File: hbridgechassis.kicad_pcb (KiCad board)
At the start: 2 copper layers, 100 x 100 mm, 8 parts, among them J1 Conn_01x02_Female, J2 Conn_01x02_Female, J3 Conn_01x02_Female, J4 Conn_01x07_Female, J5 Conn_01x02_Female, J6 Conn_01x02_Female, U1 L293DD

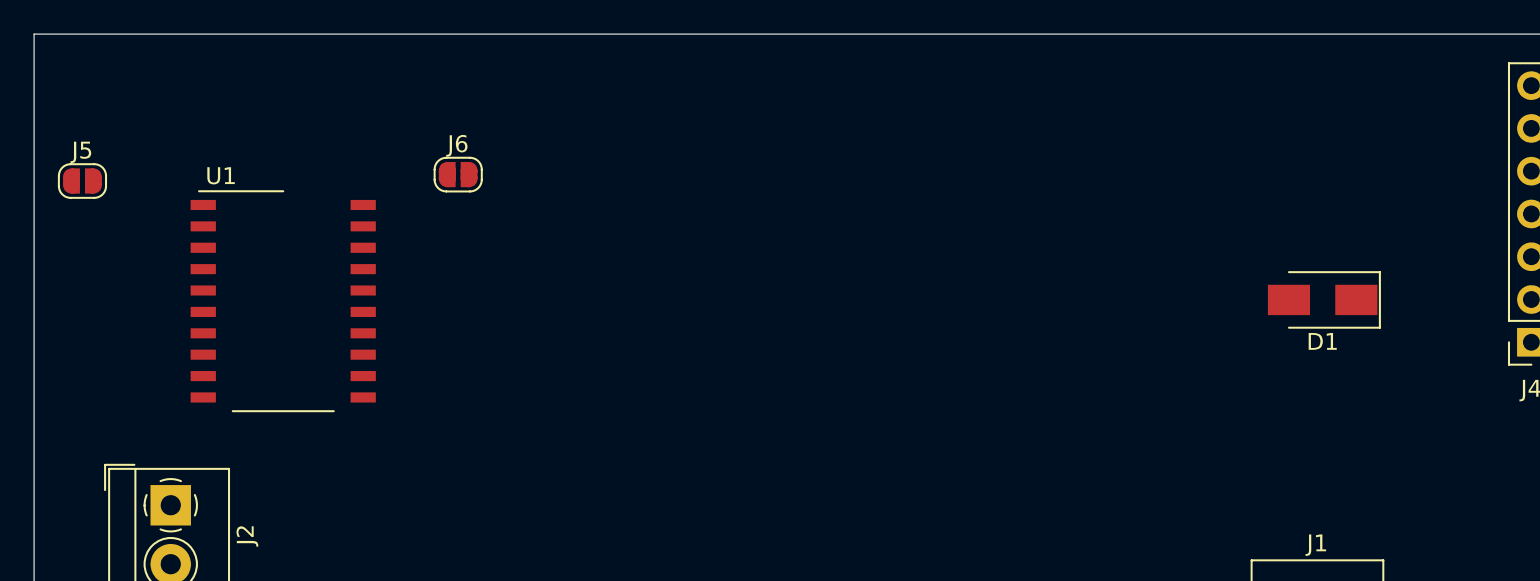
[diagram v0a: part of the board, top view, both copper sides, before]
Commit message: agregado regulador 78l05 y condensadores
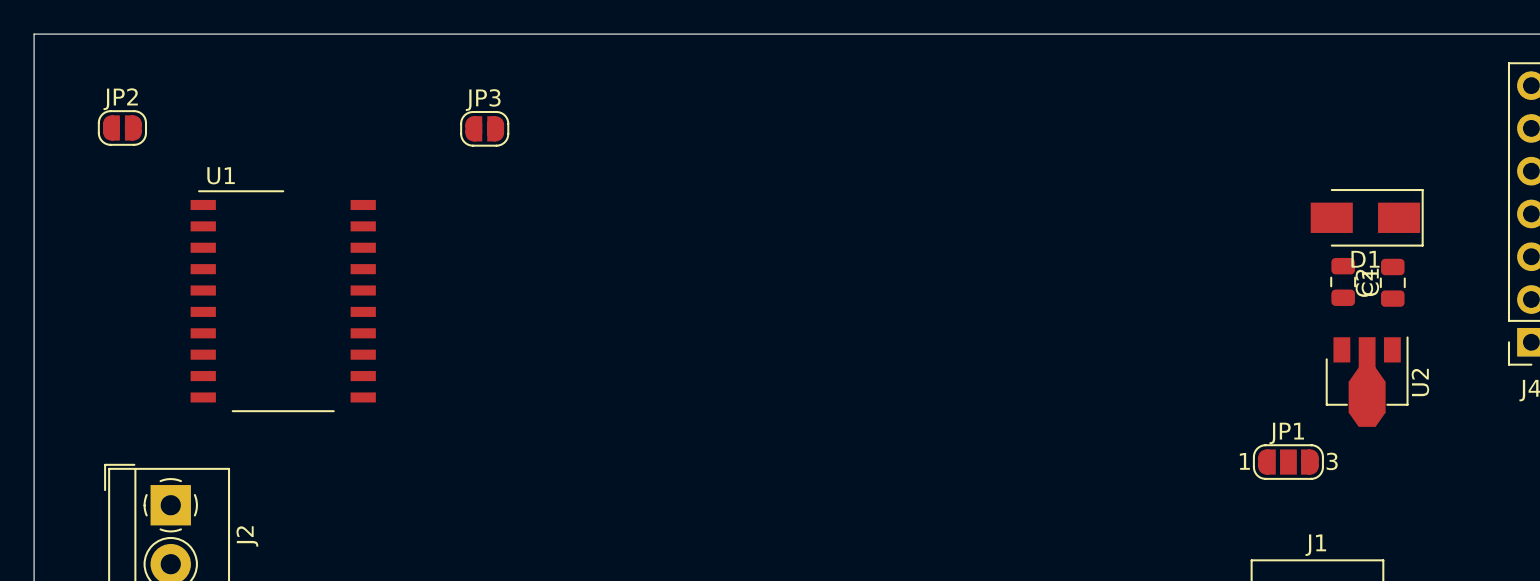
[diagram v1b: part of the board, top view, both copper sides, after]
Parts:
- removed J5, J6: Conn_01x02_Female, Jumper:SolderJumper-2_P1.3mm_Open_RoundedPad1.0x1.5mm
- added C1: C, Capacitor_SMD:C_0805_2012Metric, F.Cu at (127.7, 64.7)
- added C2: C, Capacitor_SMD:C_0805_2012Metric, F.Cu at (130.7, 64.8)
- added JP1: SolderJumper_3_Open, Jumper:SolderJumper-3_P1.3mm_Open_RoundedPad1.0x1.5mm_NumberLabels, F.Cu at (124.5, 75.4)
- added JP2: SolderJumper_2_Open, Jumper:SolderJumper-2_P1.3mm_Open_RoundedPad1.0x1.5mm, F.Cu at (55.2, 55.6)
- added JP3: SolderJumper_2_Open, Jumper:SolderJumper-2_P1.3mm_Open_RoundedPad1.0x1.5mm, F.Cu at (76.8, 55.6)
- added U2: L78L05_SOT89, Package_TO_SOT_SMD:SOT-89-3, F.Cu at (129.2, 70.2)
- moved D1 5.50 mm to (129.1, 60.9)
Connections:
- J1 pad 1: Net-(D1-Pad2) -> Net-(J1-Pad1)
- U1 pad 10: Net-(D1-Pad2) -> Net-(J1-Pad1)
- U1 pad 20: Net-(D1-Pad2) -> Net-(J1-Pad1)

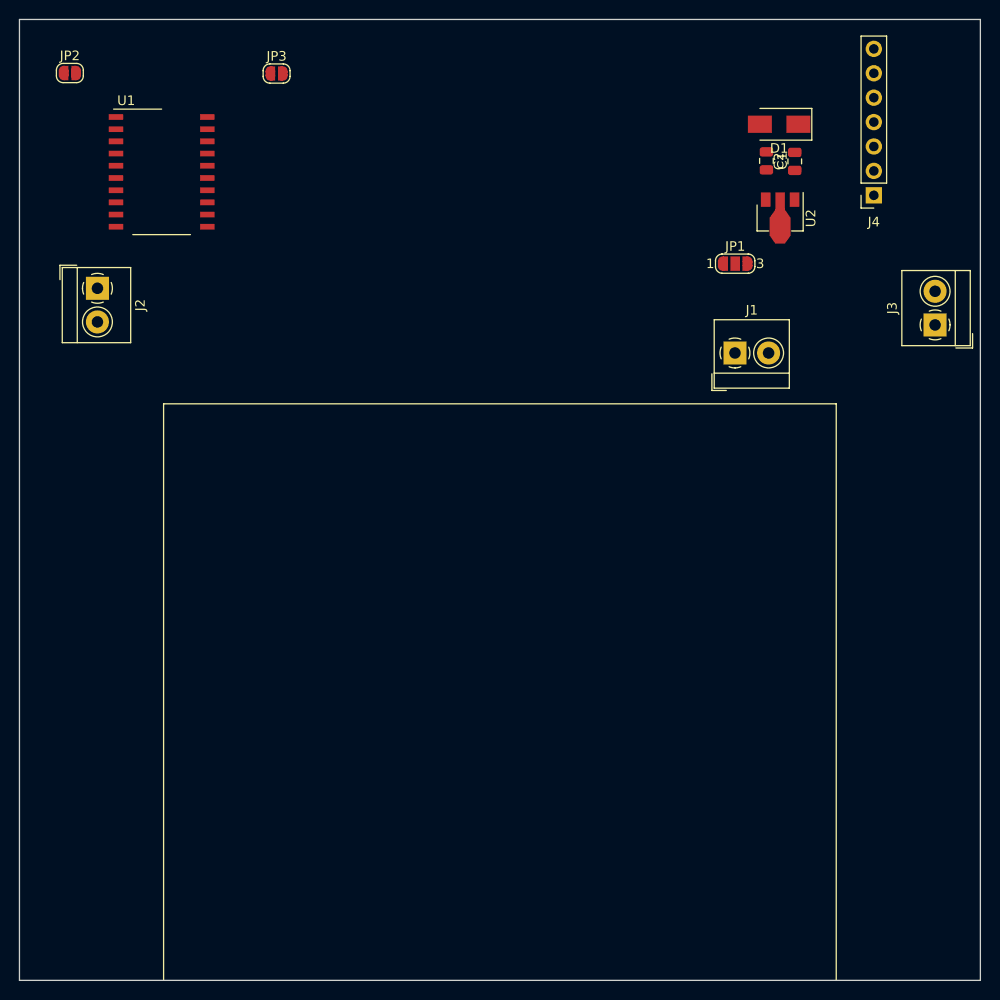
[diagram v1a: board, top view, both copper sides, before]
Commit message: enrutado preliminar de pistas y archivos de fabricacion
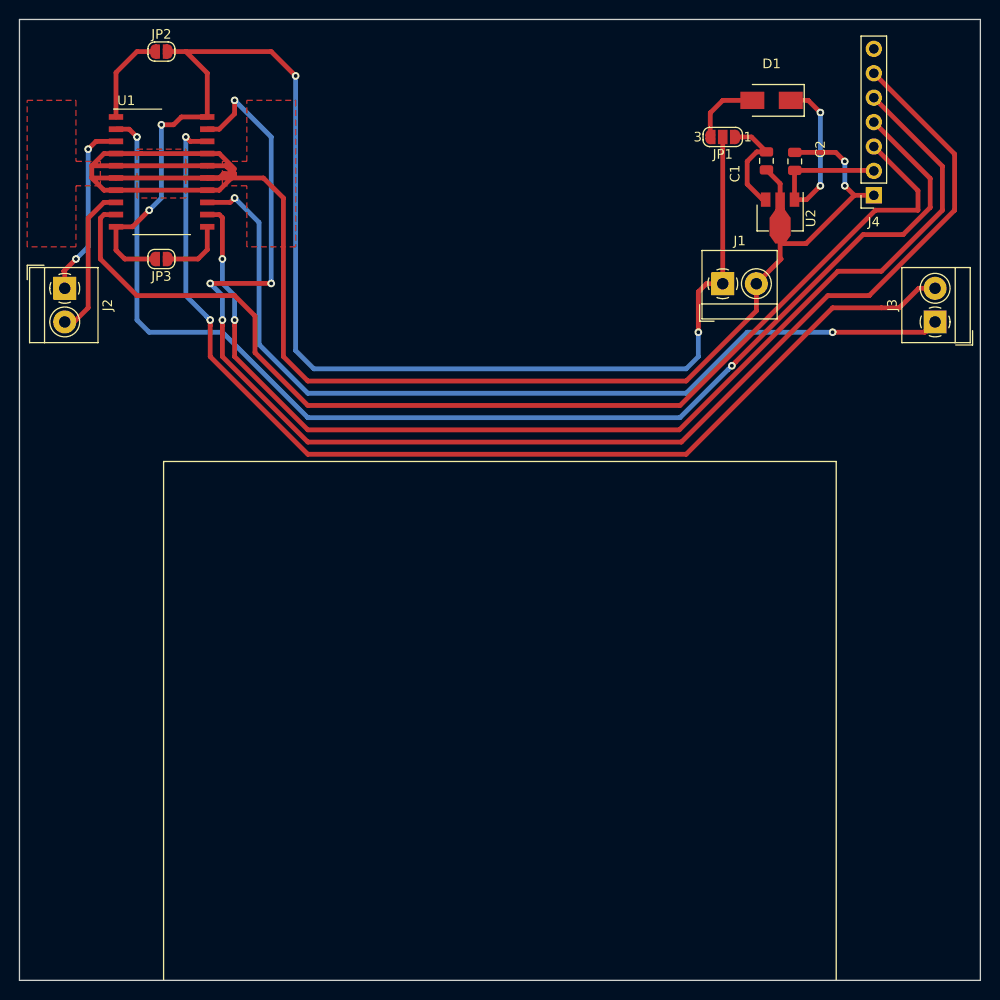
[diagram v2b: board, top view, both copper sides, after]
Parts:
- C1: value C -> 0.33uF
- C2: value C -> 0.1uF
- J1, J2, J3: value Conn_01x02_Female -> 3.5 mm screw terminal
- J4: value Conn_01x07_Female -> 2.54 mm 01x07 Female socket
- moved JP3 22.7 mm to (64.8, 74.9), turned to 180 degrees
- moved JP1 13.2 mm to (123.2, 62.2), turned to 180 degrees
- moved JP2 9.78 mm to (64.8, 53.3)
- moved J1 7.32 mm to (123.2, 77.5)
- moved J2 3.40 mm to (54.7, 78.0)
- moved D1 2.61 mm to (128.3, 58.4)
- moved J3 0.31 mm to (145.3, 81.5)
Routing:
- net Net-(C1-Pad2): track 0.00 -> 180.2 mm, vias 0 -> 2
- net Net-(J4-Pad6): track 0.00 -> 147.6 mm, vias 0 -> 4
- net Net-(J1-Pad1): track 0.00 -> 144.4 mm, vias 0 -> 4
- net Net-(J4-Pad4): track 0.00 -> 128.7 mm, vias 0 -> 2
- net Net-(J4-Pad5): track 0.00 -> 117.6 mm, vias 0 -> 2
- net Net-(J4-Pad3): track 0.00 -> 116.6 mm
- net Net-(J3-Pad2): track 0.00 -> 113.1 mm, vias 0 -> 2
- net Net-(J3-Pad1): track 0.00 -> 94.9 mm, vias 0 -> 2
- net Net-(C2-Pad1): track 0.00 -> 25.8 mm, vias 0 -> 2
- net Net-(J2-Pad1): track 0.00 -> 18.8 mm, vias 0 -> 2
- net Net-(J2-Pad2): track 0.00 -> 16.0 mm
- net Net-(C1-Pad1): track 0.00 -> 11.3 mm
- net Net-(JP2-Pad1): track 0.00 -> 9.60 mm
- net Net-(D1-Pad2): track 0.00 -> 7.43 mm
- net Net-(JP3-Pad1): track 0.00 -> 6.91 mm
- added copper zone on F.Cu, net Net-(C1-Pad2)
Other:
- net class Default: trace_width 0.25 -> 0.5

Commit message: Logo, areas de cobre y mejoras en serigrafia
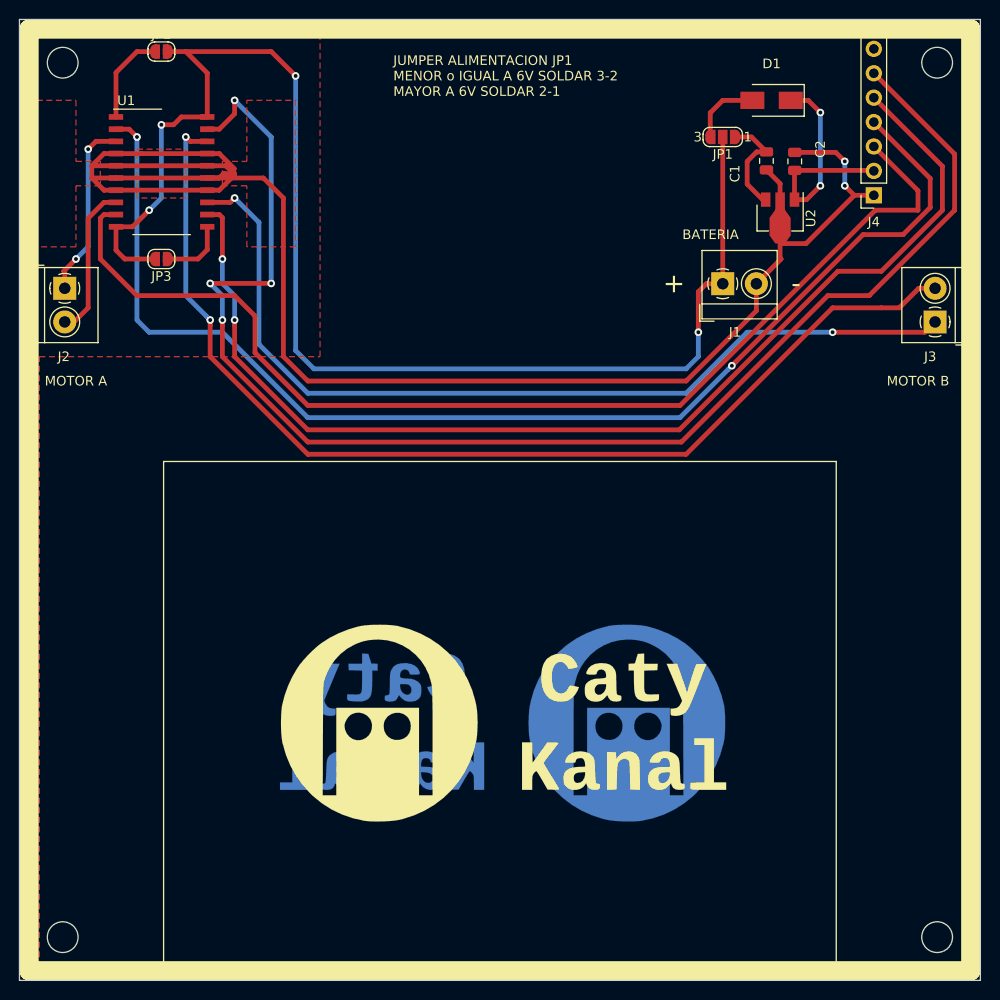
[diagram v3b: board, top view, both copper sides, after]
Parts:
- added G***: LOGO, Logos-Caty-Kanal:CATY-KANAL-Logo_47x21mm_Copper, B.Cu at (100.3, 123.2)
- added G***: LOGO, Logos-Caty-Kanal:CATY-KANAL-Logo_47x21mm_SilkScreen, F.Cu at (100.3, 123.2)
- added M1: MountingHole_3.2mm_M3, MountingHole:MountingHole_3.2mm_M3, F.Cu at (54.5, 145.5)
- added M2: MountingHole_3.2mm_M3, MountingHole:MountingHole_3.2mm_M3, F.Cu at (145.5, 145.5)
- added M3: MountingHole_3.2mm_M3, MountingHole:MountingHole_3.2mm_M3, F.Cu at (145.5, 54.5)
- added M4: MountingHole_3.2mm_M3, MountingHole:MountingHole_3.2mm_M3, F.Cu at (54.5, 54.5)
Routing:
- added copper zone on B.Cu, net Net-(C1-Pad2)
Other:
- board text added: "+"
- board text added: "-"
- board text added: "BATERIA"
- board text added: "JUMPER ALIMENTACION JP1 MENOR o IGUAL A 6V SOLDAR 3-2 MAYOR A 6V SOLDAR 2-1"
- board text added: "MOTOR A"
- board text added: "MOTOR B"
